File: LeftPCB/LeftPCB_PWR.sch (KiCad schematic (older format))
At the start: 25 parts

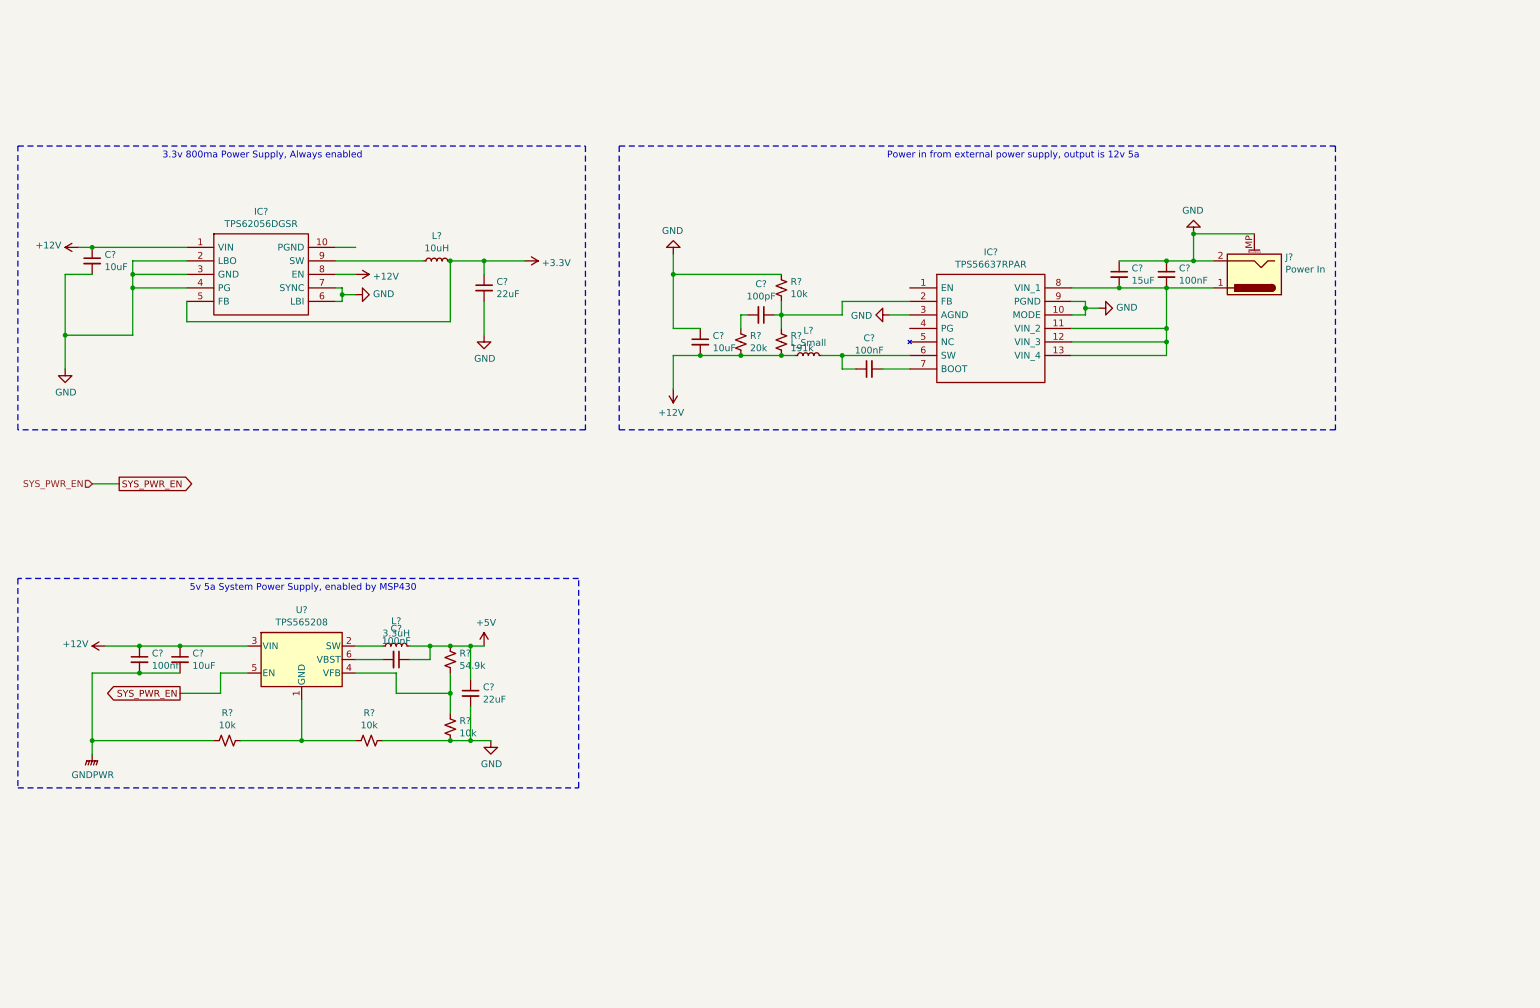
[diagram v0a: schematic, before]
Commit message: Completed most of left side schematic and started working on layout.
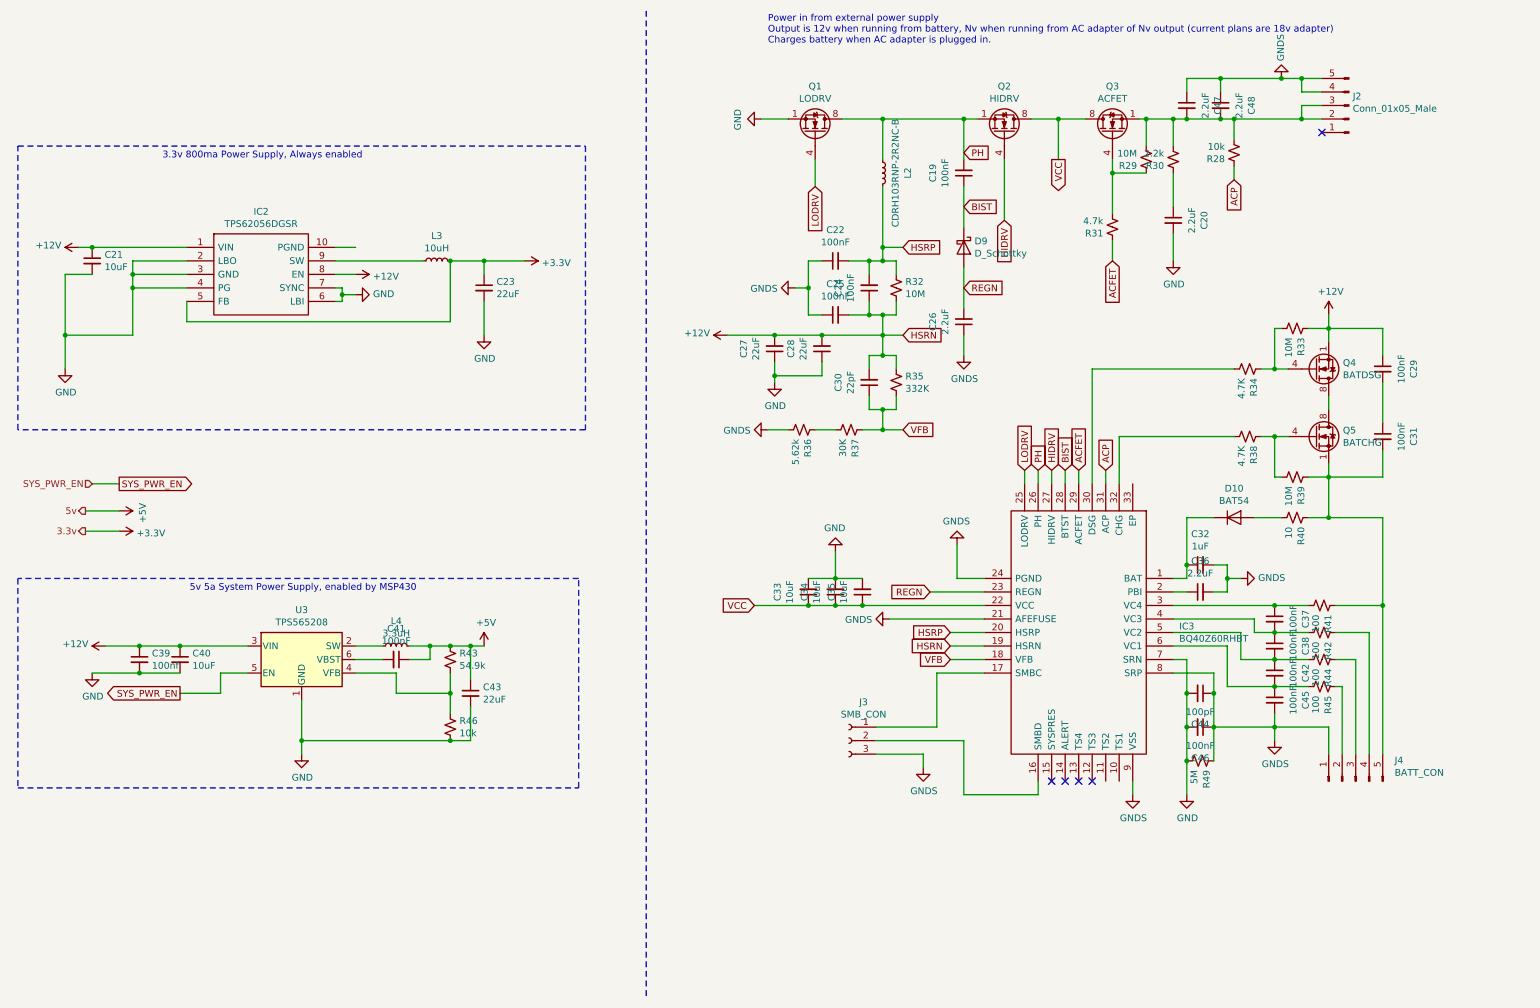
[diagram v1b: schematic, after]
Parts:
- removed C?: 15uF, symbol Device:C_Small
- removed C? (x2): 100nF, symbol Device:C_Small
- removed C?: 10uF, symbol Device:C_Small
- removed C?: 100pF, symbol Device:C_Small
- removed IC?: TPS56637RPAR, TPS56637RPAR, symbol TPS56637RPAR:TPS56637RPAR
- removed J?: Power In, symbol Connector:Barrel_Jack_MountingPin
- removed L?: L_Small, symbol Device:L_Small
- removed R?: 191k, symbol Device:R_Small_US
- removed R? (x3): 10k, symbol Device:R_Small_US
- removed R?: 20k, symbol Device:R_Small_US
- added C19, C22, C24, C25, C29, C31, C37, C38, C42, C45, C46: 100nF, Capacitors_SMD:C_0603, symbol Device:C_Small
- added C20, C26, C36, C47, C48: 2.2uF, Capacitors_SMD:C_0603, symbol Device:C_Small
- added C27, C28: 22uF, Capacitors_SMD:C_0603, symbol Device:C_Small
- added C30: 22pF, Capacitors_SMD:C_0603, symbol Device:C_Small
- added C32: 1uF, Capacitors_SMD:C_0603, symbol Device:C_Small
- added C33, C34, C35: 10uF, Capacitors_SMD:C_0603, symbol Device:C_Small
- added C44: 100pF, Capacitors_SMD:C_0603, symbol Device:C_Small
- added D10: BAT54, Diodes_SMD:D_0603, symbol Device:D
- added D9: D_Schottky, Diodes_SMD:D_0603, symbol Device:D_Schottky
- added IC3: BQ40Z60RHBT, BQ40Z60RHBT:QFN50P500X500X100-33N-D, symbol BQ40Z60:BQ40Z60RHBT
- added J2: Conn_01x05_Male, Pin_Headers:Pin_Header_Straight_1x05_Pitch1.00mm, symbol Connector:Conn_01x05_Male
- added J3: SMB_CON, Pin_Headers:Pin_Header_Straight_1x03_Pitch1.00mm, symbol Connector:Conn_01x03_Female
- added J4: BATT_CON, Pin_Headers:Pin_Header_Straight_1x05_Pitch1.00mm, symbol Connector:Conn_01x05_Male
- added L2: CDRH103RNP-2R2NC-B, Inductors_SMD:L_Vishay_IHLP-2020, symbol Device:L_Small
- added Q1: LODRV, SMD_Packages:SOIC-8-N, symbol Transistor_FET:IRF7403
- added Q2: HIDRV, SMD_Packages:SOIC-8-N, symbol Transistor_FET:IRF7403
- added Q3: ACFET, SMD_Packages:SOIC-8-N, symbol Transistor_FET:IRF7403
- added Q4: BATDSG, SMD_Packages:SOIC-8-N, symbol Transistor_FET:IRF7403
- added Q5: BATCHG, SMD_Packages:SOIC-8-N, symbol Transistor_FET:IRF7403
- added R28: 10k, Resistors_SMD:R_0603, symbol Device:R_Small_US
- added R29, R32, R33, R39: 10M, Resistors_SMD:R_0603, symbol Device:R_Small_US
- added R30: 2.2k, Resistors_SMD:R_0603, symbol Device:R_Small_US
- added R31: 4.7k, Resistors_SMD:R_0603, symbol Device:R_Small_US
- added R34, R38: 4.7K, Resistors_SMD:R_0603, symbol Device:R_Small_US
- added R35: 332K, Resistors_SMD:R_0603, symbol Device:R_Small_US
- added R36: 5.62k, Resistors_SMD:R_0603, symbol Device:R_Small_US
- added R37: 30K, Resistors_SMD:R_0603, symbol Device:R_Small_US
- added R40: 10, Resistors_SMD:R_0603, symbol Device:R_Small_US
- added R41, R42, R44, R45: 100, Resistors_SMD:R_0603, symbol Device:R_Small_US
- added R49: 5M, Resistors_SMD:R_0603, symbol Device:R_Small_US
- C21, C23, C39, C40, C41, C43: renamed from C?; footprint (none) -> Capacitors_SMD:C_0603
- IC2: renamed from IC?; footprint SOP50P490X110-10N -> TPS62056DGSR:SOP50P490X110-10N
- L3, L4: renamed from L?; footprint (none) -> Inductors_SMD:L_0603
- R43, R46: renamed from R?; footprint (none) -> Resistors_SMD:R_0603
- U3: renamed from U?; footprint Package_TO_SOT_SMD:SOT-23-6 -> TPS565208DDCR:SOT95P280X110-6N
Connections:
- net GNDPWR is gone; now on net GND: C39.2, C40.2
- net +12V: now also C24.1, C25.2, C27.2, C28.2, C29.1, C30.2, IC3.19 (HSRN), Q4.1 (S), Q4.2 (S), Q4.3 (S), R32.2, R33.1, R35.1
- net GND: now also U3.1 (GND), C20.2, C27.1, C28.1, C33.2, C34.2, C35.2, C44.2, C46.2, IC3.7 (SRN), Q1.1 (S), Q1.2 (S), Q1.3 (S), R49.2
- new net: C32.1, D10.1 (K), IC3.1 (BAT)
- new net: IC3.16 (SMBD), J3.2 (Pin_2)
- new net: IC3.17 (SMBC), J3.1 (Pin_1)
- new net: C36.1, IC3.2 (PBI)
- new net: C37.1, IC3.3 (VC4), R41.2
- new net: IC3.30 (DSG), R34.2
- new net: IC3.32 (CHG), R38.2
- new net: C37.2, C38.1, IC3.4 (VC3), R42.2
- new net: C38.2, C42.1, IC3.5 (VC2), R44.2
- new net: C42.2, C45.1, IC3.6 (VC1), R45.2
- new net: C31.2, J4.5 (Pin_5), Q5.1 (S), Q5.2 (S), Q5.3 (S), R39.1, R40.1, R41.1
- new net: D10.2 (A), R40.2
- new net: J4.2 (Pin_2), R45.1
- new net: J4.3 (Pin_3), R44.1
- new net: J4.4 (Pin_4), R42.1
- new net: Q5.4 (G), R38.1, R39.2
- new net: Q4.4 (G), R33.2, R34.1
- new net: C47.2, C48.2, J2.2 (Pin_2), J2.3 (Pin_3), Q3.1 (S), Q3.2 (S), Q3.3 (S), R28.2, R29.2, R30.2
- new net: Q3.4 (G), R29.1, R31.2
- new net: C20.1, R30.1
- new net: R36.1, R37.2
- new net: C29.2, C31.1
- new net: Q4.5 (D), Q4.6 (D), Q4.7 (D), Q4.8 (D), Q5.5 (D), Q5.6 (D), Q5.7 (D), Q5.8 (D)
- new net ACFET: IC3.29 (ACFET), R31.1
- new net ACP: IC3.31 (ACP), R28.1
- new net BIST: C19.1, D9.1 (K), IC3.28 (BTST)
- new net GNDS: C22.1, C25.1, C26.1, C32.2, C36.2, C44.1, C45.2, C46.1, C47.1, C48.1, IC3.21 (AFEFUSE), IC3.24 (PGND), IC3.8 (SRP), IC3.9 (VSS), J2.4 (Pin_4), J2.5 (Pin_5), J3.3 (Pin_3), J4.1 (Pin_1), R36.2, R49.1
- new net HIDRV: IC3.27 (HIDRV), Q2.4 (G)
- new net HSRP: C22.2, C24.2, IC3.20 (HSRP), L2.2, R32.1
- new net LODRV: IC3.25 (LODRV), Q1.4 (G)
- new net PH: C19.2, IC3.26 (PH), L2.1, Q1.5 (D), Q1.6 (D), Q1.7 (D), Q1.8 (D), Q2.1 (S), Q2.2 (S), Q2.3 (S)
- new net REGN: C26.2, D9.2 (A), IC3.23 (REGN)
- new net VCC: C33.1, C34.1, C35.1, IC3.22 (VCC), Q2.5 (D), Q2.6 (D), Q2.7 (D), Q2.8 (D), Q3.5 (D), Q3.6 (D), Q3.7 (D), Q3.8 (D)
- new net VFB: C30.1, IC3.18 (VFB), R35.2, R37.1
- no-connect marks 0 -> 5
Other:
- note added: "Power in from external power supply\nOutput is 12v when running from battery, Nv when running from AC adapter of Nv output (current plans are 18v adapter)\nCharges battery when AC adapter is plugged in."
- note removed: "Power in from external power supply, output is 12v 5a"

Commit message: Updated and performed layout on most of left PCB, still have a few things to add.
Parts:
- R49: footprint Resistors_SMD:R_0603 -> Resistors_SMD:R_2010
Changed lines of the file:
@@
 F 0 "R49" H 9668 6096 50  0000 L CNN
 F 1 "5M" H 9668 6005 50  0000 L CNN
-F 2 "Resistors_SMD:R_0603" H 9600 6050 50  0001 C CNN
+F 2 "Resistors_SMD:R_2010" H 9600 6050 50  0001 C CNN
 F 3 "~" H 9600 6050 50  0001 C CNN
 	1    9600 6050
@@
 	9750 1000 9500 1000
 $Comp
-L power:GND #PWR?
+L power:GND #PWR044
 U 1 1 5F1A354A
 P 6450 3250
-F 0 "#PWR?" H 6450 3000 50  0001 C CNN
+F 0 "#PWR044" H 6450 3000 50  0001 C CNN
 F 1 "GND" H 6455 3077 50  0000 C CNN
 F 2 "" H 6450 3250 50  0001 C CNN
